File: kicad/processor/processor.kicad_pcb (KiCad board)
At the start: 4 copper layers, 75 x 50 mm, 86 parts, among them J2 V_QI, J3 GND, J4 Battery, M1 MICROSD, Q1 DMG3415U, Q2 DMG3415U, Q3 DMG3414U, Q4 DMG3415U, Q5 DMG3415U, Q6 DMG3415U, Q7 DMG3415U, Q8 MMBT4401, Q9 MMBT4401, SW1 SW, SW2 SWITCH_PUSHBUTTON, SW3 SWITCH_PUSHBUTTON, U1 ESP32-WROOM, U2 BME280, U3 TCA9534A, U4 MCP73832, U5 NCP694-3.3, U7 USB_B_Socket, U8 SP3003-04, U9 CP2102N

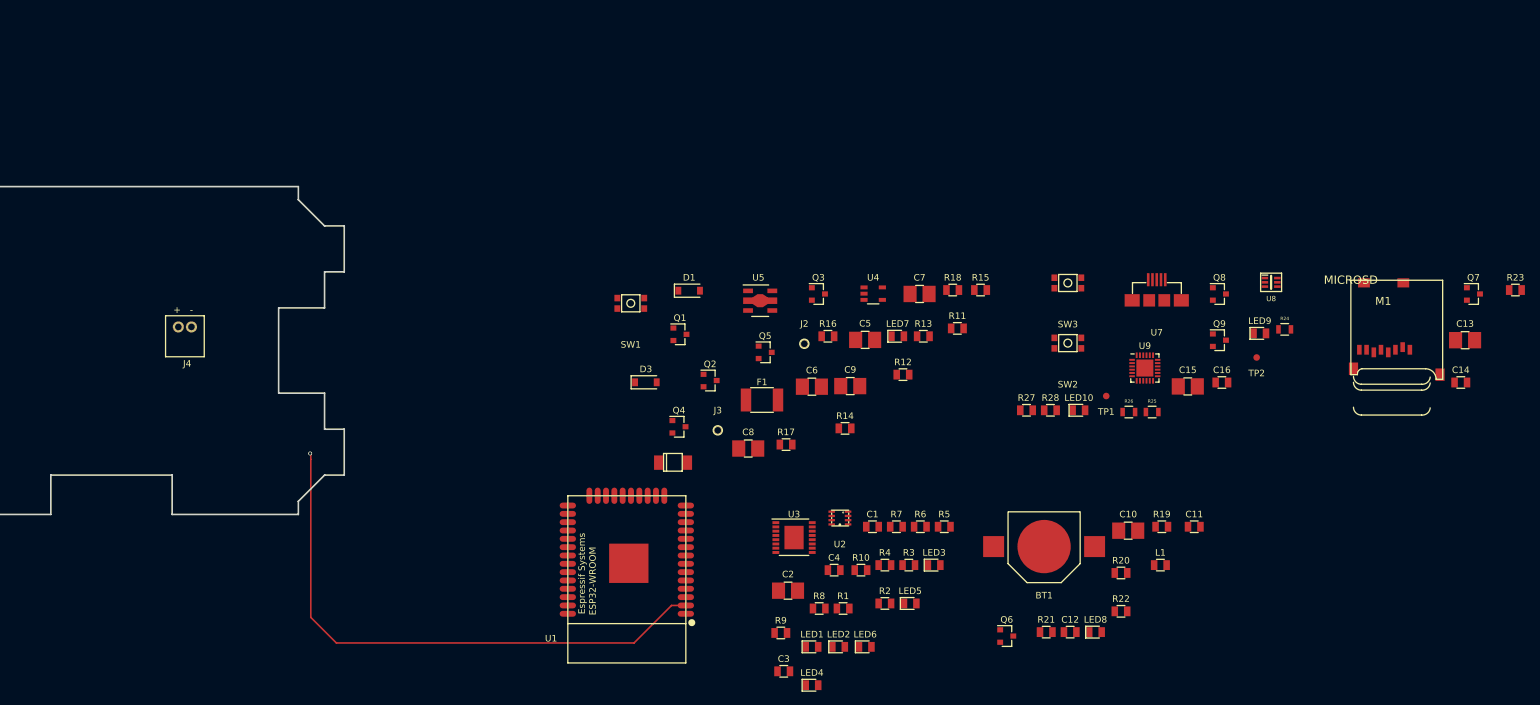
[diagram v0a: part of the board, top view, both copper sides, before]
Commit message: start processor layout - footprint fixes
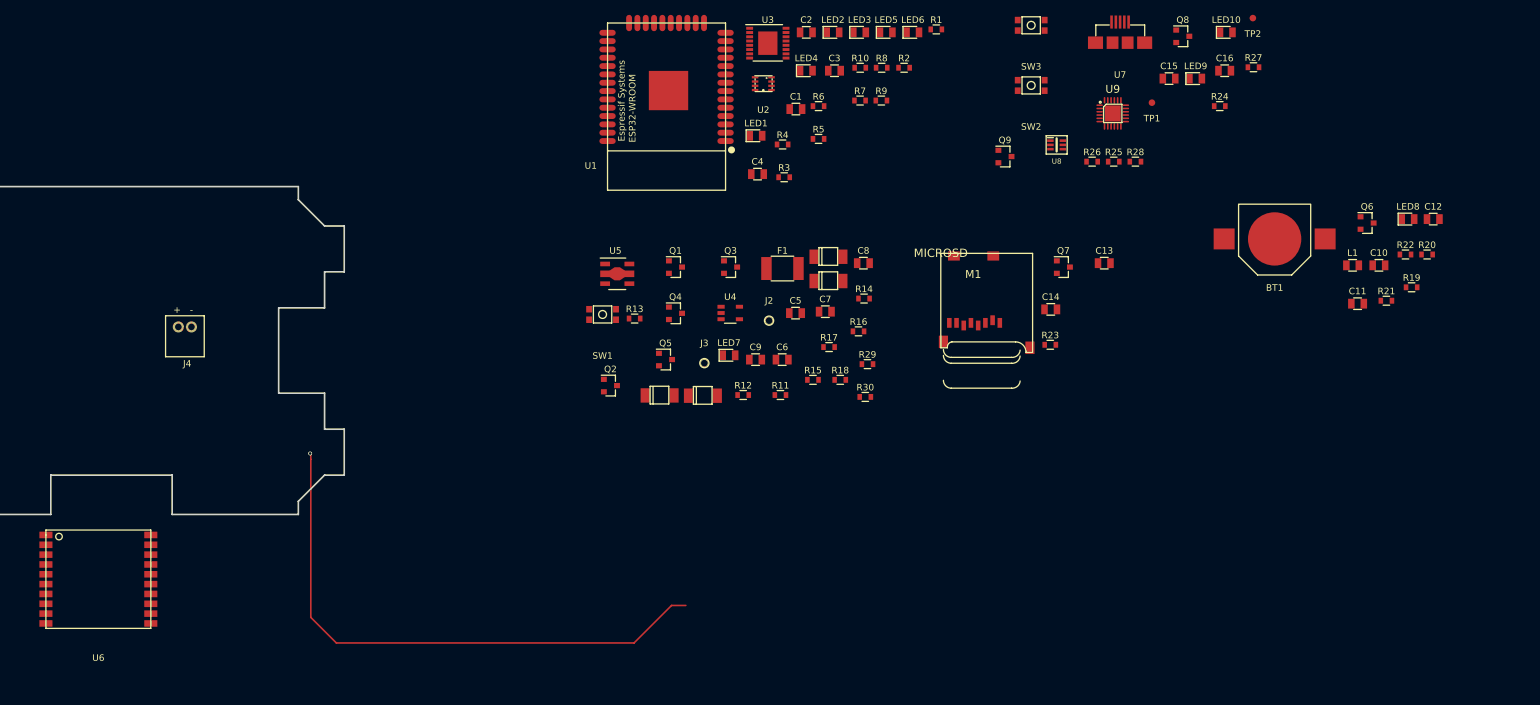
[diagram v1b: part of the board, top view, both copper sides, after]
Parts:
- added D4: RB168LAM-30, paddle:D_SOD-128, F.Cu at (179.7, 81.9)
- added R29: 1Meg, paddle:R_0603, F.Cu at (204.8, 77.1)
- added R30: 1.0k, paddle:R_0603, F.Cu at (204.5, 82.1)
- added U6: FGPMMOPA6H, paddle:FGPMMOPA6H, F.Cu at (87.5, 110.1)
- C10, C13, C15, C2, C5, C6, C7, C8, C9: footprint paddle:SMD_1206 -> paddle:SMD_0805
- D1, D3: footprint paddle:D_SOD-123 -> paddle:D_SOD-128
- R1, R10, R11, R12, R13, R14, R15, R16, R17, R19, R2, R20, R21, R22, R23, R27, R28, R3, R4, R5, R6, R7, R8, R9: footprint paddle:SMD_0805 -> paddle:R_0603
- R18: value 1Meg -> 100k; footprint paddle:SMD_0805 -> paddle:R_0603
- R24, R25, R26: footprint paddle:R_0805 -> paddle:R_0603
- U9: footprint paddle:QFN-24-1EP_4x4mm_Pitch0.5mm -> paddle:QFP_24
- moved LED6 94.0 mm to (211.7, 26.5)
- moved LED2 93.7 mm to (199.5, 26.5)
- moved LED4 93.7 mm to (195.5, 32.3)
- moved C3 91.9 mm to (199.8, 32.3)
- moved R1 89.5 mm to (215.3, 26.0)
- moved LED5 87.2 mm to (207.7, 26.5)
- moved C2 85.2 mm to (195.5, 26.5)
- moved C12 83.9 mm to (291.1, 55.0)
- moved Q6 83.6 mm to (281.0, 55.6)
- moved R8 83.0 mm to (207.0, 31.9)
- moved R9 82.6 mm to (206.9, 36.9)
- moved LED3 82.0 mm to (203.6, 26.5)
- moved R2 81.8 mm to (210.4, 31.9)
- moved LED8 79.0 mm to (287.2, 55.0)
- moved LED1 78.4 mm to (187.8, 42.2)
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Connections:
- net /sheet59FFAB61/CS renamed /SD_CS*
- C6 pad 1: /KEEPALIVE -> Net-(C6-Pad1)
- D3 pad 1: Net-(D3-Pad1) -> /KEEPALIVE
- D3 pad 2: /POWER_SW* -> Net-(C6-Pad1)
- Q3 pad 1: /KEEPALIVE -> Net-(C6-Pad1)
- Q3 pad 3: Net-(D3-Pad1) -> Net-(Q3-Pad3)
- Q4 pad 1: Net-(D3-Pad1) -> Net-(Q3-Pad3)
- R14 pad 2: /KEEPALIVE -> Net-(C6-Pad1)
- R15 pad 1: Net-(D3-Pad1) -> Net-(Q3-Pad3)
- R18 pad 2: /+V_UNREG_SW -> Net-(D4-Pad1)
- R20 pad 2: (no net) -> Net-(R20-Pad2)
- R21 pad 2: (no net) -> Net-(R21-Pad2)
- R22 pad 2: (no net) -> Net-(R22-Pad2)
- R28 pad 1: Net-(Q8-Pad1) -> Net-(Q9-Pad2)
- R28 pad 2: Net-(Q9-Pad2) -> Net-(Q8-Pad1)
- SW1 pad 1: /POWER_SW* -> Net-(D4-Pad1)
- SW1 pad 2: GND -> Net-(D1-Pad2)
- U1 pad 10: (no net) -> /BUSY*
- U1 pad 11: /BLINK -> (no net)
- U1 pad 16: (no net) -> /BLINK
- U1 pad 4: (no net) -> /1PPS
- U1 pad 5: /BUSY* -> (no net)
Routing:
- net +3V3: track 86.2 -> 0.00 mm, vias 1 -> 0
- net (no net): track 0.00 -> 86.2 mm, vias 0 -> 1

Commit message: First cut layout power supply, fix netclasses, footprint for connector
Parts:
- removed LED1, LED10, LED2, LED3, LED4, LED5, LED6, LED7, LED8, LED9: LED, paddle:SMD_D_0805
- removed U9: CP2102N, paddle:QFP_24
- added J101: CONN_02X07, paddle:conn_FCI_14, F.Cu at (44.2, 42.0)
- added LED101: LED, paddle:SMD_D_0805, F.Cu at (234.9, 54.5)
- added LED102: LED, paddle:SMD_D_0805, F.Cu at (240.9, 60.4)
- added LED103: LED, paddle:SMD_D_0805, F.Cu at (247.5, 48.2)
- added LED104: LED, paddle:SMD_D_0805, F.Cu at (240.9, 54.5)
- added LED105: LED, paddle:SMD_D_0805, F.Cu at (234.9, 60.4)
- added LED106: LED, paddle:SMD_D_0805, F.Cu at (241.6, 48.2)
- added LED201: LED, paddle:SMD_D_0805, F.Cu at (101.6, 60.5)
- added LED301: LED, paddle:SMD_D_0805, F.Cu at (14.8, 85.5)
- added LED501: LED, paddle:SMD_D_0805, F.Cu at (179.1, 54.3)
- added LED502: LED, paddle:SMD_D_0805, F.Cu at (170.9, 61.3)
- added REF**: hole, paddle:KH_F20_mounting_hole, F.Cu at (112.5, 55.0)
- added U503: CP2102N, paddle:QFP_24, F.Cu at (142.6, 57.8)
- BT301: renamed from BT1; moved to B.Cu
- D201: renamed from D3; value RB168LAM-30 -> SS24FL; footprint paddle:D_SOD-128 -> paddle:D_SOD-123
- D202: renamed from D4; value RB168LAM-30 -> SS24FL; footprint paddle:D_SOD-128 -> paddle:D_SOD-123
- D203: renamed from D1; value RB168LAM-30 -> SS24FL; footprint paddle:D_SOD-128 -> paddle:D_SOD-123
- D204: renamed from D2; value RB168LAM-30 -> SS24FL; footprint paddle:D_SOD-128 -> paddle:D_SOD-123
- J203: renamed from J4; moved to B.Cu
- moved C303 268.7 mm to (24.1, 85.5)
- moved C301 264.0 mm to (19.9, 85.5)
- moved R302 262.9 mm to (28.4, 85.1)
- moved R303 250.6 mm to (33.7, 81.9)
- moved R301 250.2 mm to (37.9, 76.1)
- moved Q301 245.6 mm to (35.8, 70.1)
- moved L301 245.6 mm to (33.6, 76.5)
- moved R304 239.4 mm to (47.6, 69.0)
- moved C302 236.8 mm to (42.7, 69.5)
- moved BT301 211.8 mm to (55.6, 72.2), turned to 270 degrees
- moved C104 121.0 mm to (67.5, 58.5), turned to 180 degrees
- moved R102 118.9 mm to (105.8, 88.2), turned to 270 degrees
- moved U103 115.8 mm to (74.0, 33.7)
- moved Q501 112.2 mm to (143.6, 52.4)
- moved R504 109.3 mm to (162.9, 74.0)
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- renumbered C1 to C101, C2 to C102, C3 to C103, C4 to C104, C5 to C201, C6 to C202, C7 to C203, C8 to C204, C9 to C205, C10 to C301, C11 to C302, C12 to C303, C13 to C401, C14 to C402, C15 to C501, C16 to C502, F1 to F201, J2 to J201, J3 to J202, L1 to L301, M1 to M401, Q1 to Q201, Q2 to Q202, Q3 to Q203, Q4 to Q204, Q5 to Q205, Q6 to Q301, Q7 to Q401, Q8 to Q501, Q9 to Q502, R1 to R101, R2 to R102, R3 to R103, R4 to R104, R5 to R105, R6 to R106, R7 to R107, R8 to R108, R9 to R109, R10 to R110, R11 to R201, R12 to R202, R13 to R203, R18 to R204, R29 to R205, R30 to R206, R14 to R207, R15 to R208, R16 to R209, R17 to R210, R19 to R301, R20 to R302, R21 to R303, R22 to R304, R23 to R401, R24 to R501, R25 to R502, R26 to R503, R27 to R504, R28 to R505, SW1 to SW201, SW2 to SW501, SW3 to SW502, TP1 to TP501, TP2 to TP502, U1 to U101, U2 to U102, U3 to U103, U4 to U201, U5 to U202, U6 to U301, U7 to U501, U8 to U502
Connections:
- net /sheet59FFAB5F/+VBUS renamed /USB/+VBUS
- net Net-(C5-Pad1) renamed /power/V+EXT
- net Net-(C7-Pad1) renamed /power/V+BAT_FUSED
- net Net-(D1-Pad2) renamed /power/V_UNREG
- net Net-(F1-Pad2) renamed /power/V+BAT
- R105 pad 2: (no net) -> Net-(LED101-Pad2)
- R106 pad 2: (no net) -> Net-(LED102-Pad2)
- R107 pad 2: (no net) -> Net-(LED103-Pad2)
- R108 pad 2: (no net) -> Net-(LED104-Pad2)
- R109 pad 2: (no net) -> Net-(LED105-Pad2)
- R110 pad 2: (no net) -> Net-(LED106-Pad2)
- R203 pad 2: (no net) -> Net-(LED201-Pad2)
- R304 pad 1: (no net) -> Net-(LED301-Pad2)
- R502 pad 2: (no net) -> Net-(LED501-Pad2)
- R503 pad 2: (no net) -> Net-(LED502-Pad2)
- U101 pad 12: (no net) -> /AN0_CS*
- U101 pad 24: (no net) -> /AN3_CS*
- U101 pad 8: (no net) -> /AN1_CS*
- U101 pad 9: (no net) -> /AN2_CS*
- U103 pad 12: (no net) -> /AN_REFSEL
- U103 pad 9: (no net) -> /+3.3VA_ENABLE
- U201 pad 1: (no net) -> Net-(LED201-Pad1)
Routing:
- net (no net): track 86.2 -> 0.00 mm, vias 1 -> 0
- net /KEEPALIVE: track 0.00 -> 43.8 mm, vias 0 -> 2
- net Net-(C202-Pad1): track 0.00 -> 38.4 mm, vias 0 -> 2
- net /+V_UNREG_SW: track 0.00 -> 38.1 mm
- net /power/V+BAT_FUSED: track 0.00 -> 32.5 mm, vias 0 -> 2
- net /POWER_SW*: track 0.00 -> 28.2 mm, vias 0 -> 2
- net /power/V+EXT: track 0.00 -> 26.3 mm
- net /power/V_UNREG: track 0.00 -> 22.6 mm, vias 0 -> 2
- net Net-(D202-Pad1): track 0.00 -> 18.5 mm
- net GND: track 0.00 -> 18.2 mm, vias 0 -> 13
- net Net-(Q203-Pad3): track 0.00 -> 17.3 mm, vias 0 -> 2
- net Net-(J201-Pad1): track 0.00 -> 13.4 mm, vias 0 -> 2
- net /power/V+BAT: track 0.00 -> 8.83 mm
- net /USB/+VBUS: track 0.00 -> 8.53 mm
- net +3V3: track 0.00 -> 5.86 mm, vias 0 -> 1
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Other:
- net class Default: clearance 0.2 -> 0.15
- net class Power added: clearance 0.15, trace_width 0.45, via_dia 0.8, via_drill 0.5
- rule trace_clearance: 0.2 -> 0.15

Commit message: Processor board routed, conn_FCI_14 switched to no hole version, port expander package fixed
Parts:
- added REF**: hole, paddle:KH_F20_mounting_hole, F.Cu at (62.5, 55.0)
- added REF**: hole, paddle:KH_F20_mounting_hole, F.Cu at (112.5, 95.0)
- added REF**: hole, paddle:KH_F20_mounting_hole, F.Cu at (62.5, 95.0)
- J101: footprint paddle:conn_FCI_14 -> paddle:conn_FCI_14_NH; moved to B.Cu
- U103: footprint paddle:TSSOP-16-1EP_4.4x5mm_Pitch0.65mm -> paddle:SOIC-16
- moved R105 181.6 mm to (76.4, 87.5), turned to 90 degrees
- moved C401 172.7 mm to (58.4, 53.6)
- moved C101 168.7 mm to (84.1, 55.0)
- moved R101 166.3 mm to (84.3, 53.1), turned to 180 degrees
- moved C402 164.1 mm to (58.0, 55.7)
- moved C102 161.8 mm to (101.2, 92.3), turned to 270 degrees
- moved LED101 161.4 mm to (76.3, 84.4), turned to 270 degrees
- moved Q401 158.2 mm to (66.5, 52.0), turned to 270 degrees
- moved R110 157.6 mm to (106.3, 77.0), turned to 90 degrees
- moved R107 156.9 mm to (108.3, 77.0), turned to 90 degrees
- moved R401 151.6 mm to (69.2, 51.9), turned to 90 degrees
- moved R109 150.6 mm to (110.3, 77.0), turned to 90 degrees
- moved R106 148.1 mm to (106.3, 89.9), turned to 270 degrees
- moved C103 147.8 mm to (103.4, 92.3), turned to 270 degrees
- moved R108 144.1 mm to (112.3, 77.0), turned to 90 degrees
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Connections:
- J101 pad 1: GND -> /SPI_SDO
- J101 pad 10: /AN_REFSEL -> /BUSY*
- J101 pad 11: /AN0_CS* -> /AN3_CS*
- J101 pad 12: /I2C_SDA -> /AN0_CS*
- J101 pad 14: /I2C_SCK -> GND
- J101 pad 2: /BUSY* -> /+3.3VA_ENABLE
- J101 pad 3: /+3.3VA_ENABLE -> /I2C_SCK
- J101 pad 4: /SPI_SCLK -> /AN1_CS*
- J101 pad 5: /AN3_CS* -> /I2C_SDA
- J101 pad 6: /SPI_SDO -> /AN2_CS*
- J101 pad 7: /AN2_CS* -> /SPI_SDI
- J101 pad 8: /SPI_SDI -> /AN_REFSEL
- J101 pad 9: /AN1_CS* -> /SPI_SCLK
- U502 pad 1: (no net) -> /USB/+VBUS
- U502 pad 5: +3V3 -> (no net)
- U502 pad 6: /USB/+VBUS -> (no net)
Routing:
- net GND: track 18.2 -> 136.9 mm, vias 13 -> 49
- net /SD_ENABLE*: track 0.00 -> 66.9 mm, vias 0 -> 6
- net /I2C_SDA: track 0.00 -> 59.9 mm, vias 0 -> 3
- net /RESET_ESP*: track 0.00 -> 54.3 mm, vias 0 -> 2
- net /1PPS: track 0.00 -> 53.7 mm, vias 0 -> 2
- net /SPI_SDO: track 0.00 -> 53.5 mm, vias 0 -> 3
- net /GPS_ENABLE*: track 0.00 -> 50.8 mm, vias 0 -> 4
- net /I2C_SCK: track 0.00 -> 48.5 mm, vias 0 -> 3
- net /SPI_SDI: track 0.00 -> 44.5 mm, vias 0 -> 3
- net /SPI_SCLK: track 0.00 -> 42.2 mm, vias 0 -> 3
- net +3V3: track 5.86 -> 39.4 mm, vias 1 -> 18
- net /SD_CS*: track 0.00 -> 30.7 mm, vias 0 -> 2
- net /CON_TXD: track 0.00 -> 30.2 mm, vias 0 -> 3
- net /+V_UNREG_SW: track 38.1 -> 67.7 mm, vias 0 -> 1
- net /USB/+VBUS: track 8.53 -> 36.6 mm, vias 0 -> 4
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
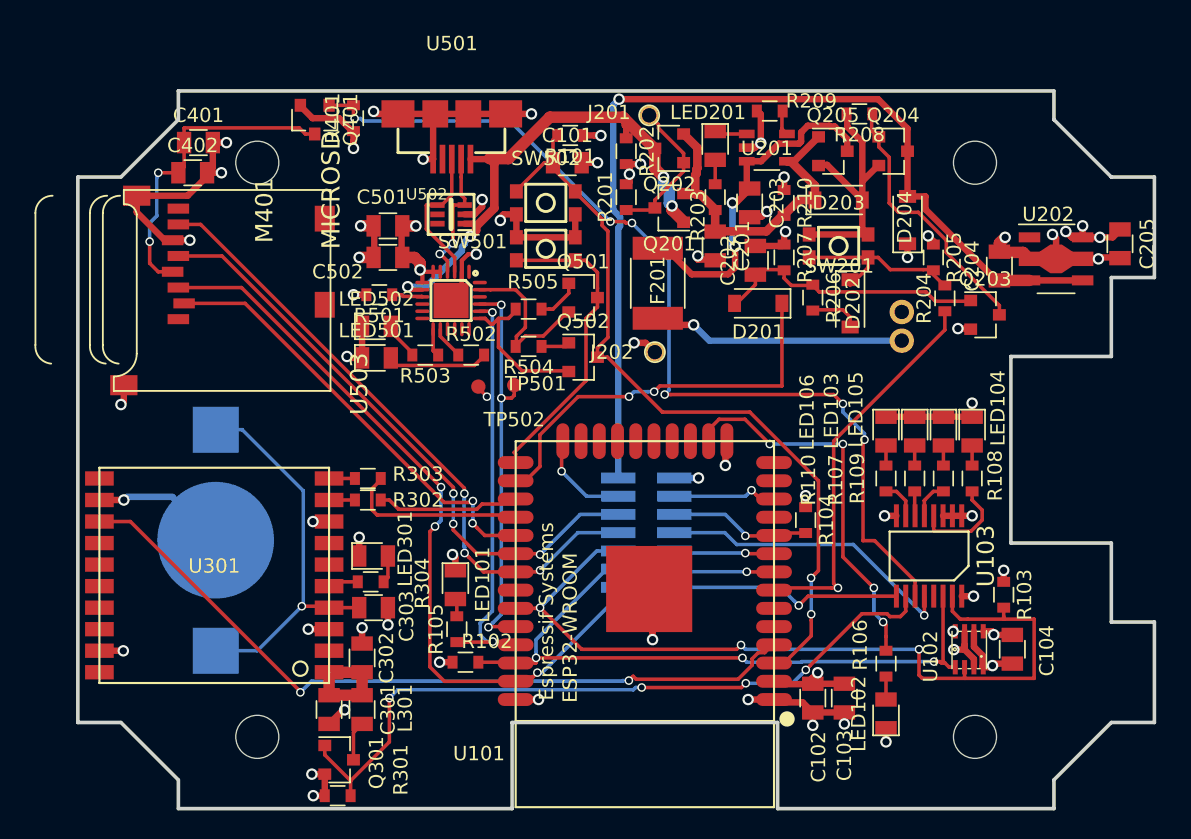
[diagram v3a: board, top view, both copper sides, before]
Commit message: Fixed components under screws, silkscreen, exported gerbers
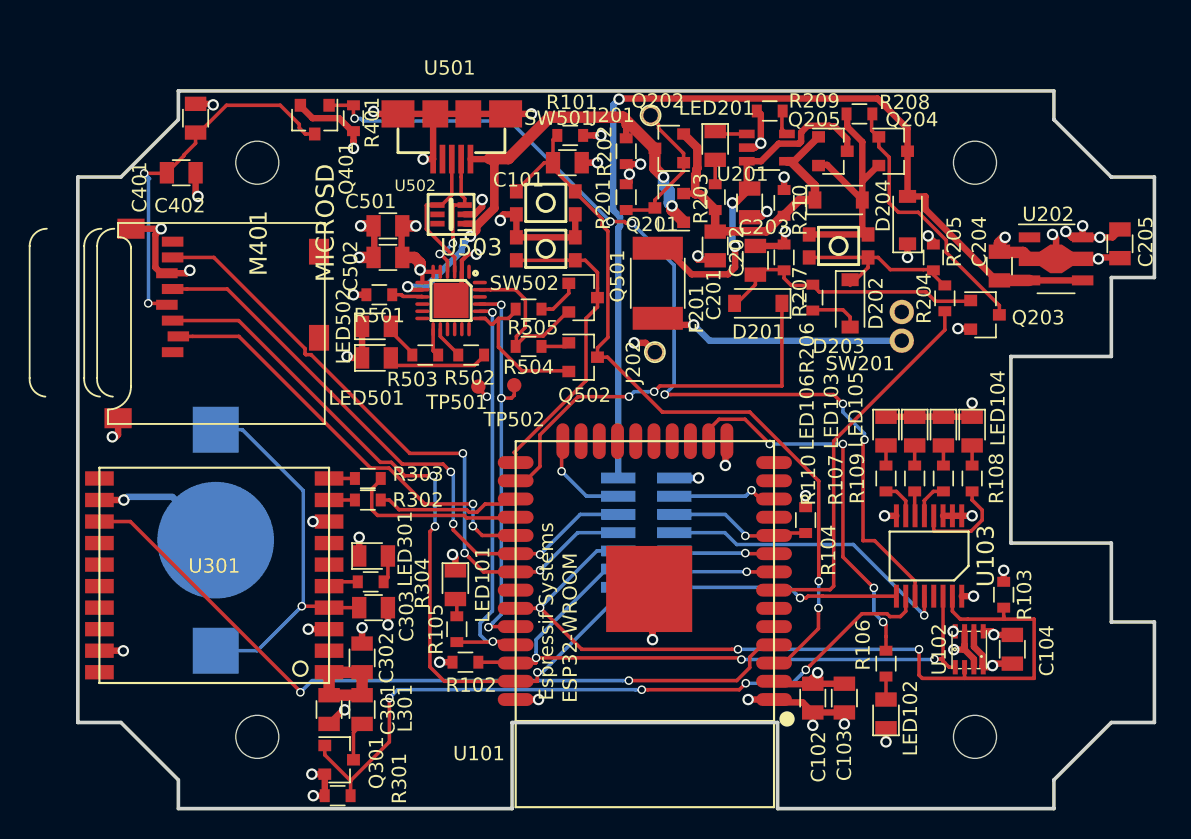
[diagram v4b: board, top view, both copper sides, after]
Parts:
- moved M401 2.33 mm to (67.2, 59.2)
- moved C401 1.71 mm to (58.2, 51.9), turned to 90 degrees
- moved C402 0.80 mm to (57.2, 55.7)
- moved J201 0.10 mm to (89.9, 51.7)
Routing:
- net GND: track 136.9 -> 132.1 mm, vias 49 -> 50
- net Net-(C401-Pad1): track 22.3 -> 26.0 mm
- net /SPI_SDI: track 44.5 -> 45.9 mm
- net Net-(J201-Pad1): track 10.4 -> 11.1 mm
- net /SD_CS*: track 30.7 -> 30.2 mm
- net /POWER_SW*: track 27.2 -> 26.7 mm, vias 1 -> 0
